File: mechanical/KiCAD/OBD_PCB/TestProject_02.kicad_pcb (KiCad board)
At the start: 2 copper layers, 41 x 58 mm, 46 parts, among them J1 USB_C_Receptacle_USB2.0_16P, J2 C-OBD-II-16M, J3 TXD_PAD, J4 RXD_PAD, U1 ESP32-C3-WROOM-02, U2 TPS54302, U3 USBLC6-2P6, U4 SN65HVD231

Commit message: Small layout changes, relocated the OBD PCB files to it's own folder. Final checks are needed.
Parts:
- moved C8 0.60 mm to (84.7, 54.4)
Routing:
- net OPMODE: track 36.3 -> 37.4 mm
- net +3.3V: track 94.7 -> 95.7 mm
- net Net-(J1-SHIELD): track 24.6 -> 25.3 mm
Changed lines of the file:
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@@
 	(footprint "Capacitor_SMD:C_0603_1608Metric"
 		(layer "B.Cu")
-		(at 84.65 53.8)
+		(at 84.7 54.4)
 		(descr "Capacitor SMD 0603 (1608 Metric), square (rectangular) end terminal, IPC-7351 nominal, (Body size source: IPC-SM-782 page 76, https://www.pcb-3d.com/wordpress/wp-content/uploads/ipc-sm-782a_amendment_1_and_2.pdf)")
 		(tags "capacitor")
@@
 		(layer "F.Fab")
 		(pts
-			(xy 46 50.4) (xy 46 97.85)
+			(xy 46 50.4) (xy 45.25 98)
 		)
 		(height -5)
@@
 			(extension_offset 0.5)
 		)
-		(gr_text "47.45mm"
-			(at 39.85 74.125 0)
+		(gr_text "47.6mm"
+			(at 39.85 74.2 0)
+			(layer "F.Fab")
+			(effects
+				(font
+					(size 1 1)
+					(thickness 0.15)
+				)
+			)
+		)
+	)
+	(dimension
+		(type orthogonal)
+		(layer "F.Fab")
+		(pts
+			(xy 87.5 119) (xy 86.75 40)
+		)
+		(height 5)
+		(orientation 1)
+		(format
+			(prefix "")
+			(suffix "mm")
+			(units 3)
+			(units_format 0)
+			(precision 4)
+			(suppress_zeroes yes)
+		)
+		(style
+			(thickness 0.05)
+			(arrow_length 1.27)
+			(text_position_mode 0)
+			(arrow_direction outward)
+			(extension_height 0.58642)
+			(extension_offset 0.5)
+		)
+		(gr_text "79mm"
+			(at 91.35 79.5 0)
 			(layer "F.Fab")
 			(effects
@@
 		(layer "F.Fab")
 		(pts
-			(xy 87 98) (xy 87 40)
+			(xy 92.5 98) (xy 92.5 40)
 		)
 		(height 5)
@@
 		)
 		(gr_text "58mm"
-			(at 90.85 69 0)
+			(at 96.35 69 0)
 			(layer "F.Fab")
 			(effects
@@
 	)
 	(segment
-		(start 49.3875 66.7)
-		(end 49.3875 75.55)
-		(width 0.5)
-		(layer "F.Cu")
-		(net "+3.3V")
-	)
-	(segment
-		(start 66.4125 70.6)
-		(end 66.4125 80.4875)
+		(start 65.45 83.3)
+		(end 63.6 83.3)
 		(width 0.5)
 		(layer "F.Cu")
@@
 	)
 	(segment
-		(start 63.6 83.3)
-		(end 61.4 85.5)
+		(start 49.3875 66.7)
+		(end 49.3875 75.55)
 		(width 0.5)
 		(layer "F.Cu")
@@
 	)
 	(segment
+		(start 67.5 85.35)
+		(end 65.45 83.3)
+		(width 0.5)
+		(layer "F.Cu")
+		(net "+3.3V")
+	)
+	(segment
+		(start 69.6 85.35)
+		(end 67.5 85.35)
+		(width 0.5)
+		(layer "F.Cu")
+		(net "+3.3V")
+	)
+	(segment
 		(start 49.3875 75.55)
 		(end 49.3875 80.9875)
@@
 	)
 	(segment
-		(start 49.3875 80.9875)
-		(end 51.7 83.3)
+		(start 66.4125 70.6)
+		(end 66.4125 82.3375)
 		(width 0.5)
 		(layer "F.Cu")
@@
 	)
 	(segment
-		(start 69.6 85.35)
-		(end 65.65 85.35)
+		(start 49.3875 80.9875)
+		(end 51.7 83.3)
 		(width 0.5)
 		(layer "F.Cu")
@@
 	)
 	(segment
-		(start 66.4125 80.4875)
-		(end 63.6 83.3)
-		(width 0.5)
-		(layer "F.Cu")
-		(net "+3.3V")
-	)
-	(segment
-		(start 61.4 85.5)
-		(end 61 85.5)
+		(start 63.25 85.5)
+		(end 65.45 83.3)
 		(width 0.5)
 		(layer "F.Cu")
@@
 	)
 	(segment
-		(start 65.65 85.35)
-		(end 63.6 83.3)
+		(start 66.4125 82.3375)
+		(end 65.45 83.3)
+		(width 0.5)
+		(layer "F.Cu")
+		(net "+3.3V")
+	)
+	(segment
+		(start 61 85.5)
+		(end 63.25 85.5)
 		(width 0.5)
 		(layer "F.Cu")
@@
 	)
 	(segment
-		(start 85.425 53.8)
-		(end 85.425 51.1125)
+		(start 85.425 51.1125)
+		(end 85.4125 51.1)
 		(width 0.5)
 		(layer "B.Cu")
@@
 	)
 	(segment
-		(start 76.79 42.425)
-		(end 85.43 42.425)
+		(start 85.475 54.4)
+		(end 85.425 54.35)
 		(width 0.5)
 		(layer "B.Cu")
@@
 	)
 	(segment
-		(start 85.425 51.1125)
-		(end 85.4125 51.1)
+		(start 76.79 42.425)
+		(end 85.43 42.425)
 		(width 0.5)
 		(layer "B.Cu")
@@
 	)
 	(segment
+		(start 85.425 54.35)
+		(end 85.425 51.1125)
+		(width 0.5)
+		(layer "B.Cu")
+		(net "Net-(J1-SHIELD)")
+	)
+	(segment
 		(start 72.6 96)
 		(end 70.6 94)
@@
 	)
 	(segment
-		(start 49.895 83.075)
-		(end 49.895 82.100001)
+		(start 72 63.2)
+		(end 71.5 63.2)
 		(width 0.25)
 		(layer "B.Cu")
@@
 	)
 	(segment
-		(start 60 81.2)
-		(end 71.5 69.7)
+		(start 72.5 63.7)
+		(end 72 63.2)
 		(width 0.25)
 		(layer "B.Cu")
@@
 	)
 	(segment
-		(start 71.5 69.7)
-		(end 71.5 63.2)
+		(start 50.795001 81.2)
+		(end 60 81.2)
 		(width 0.25)
 		(layer "B.Cu")
@@
 	)
 	(segment
-		(start 50.795001 81.2)
-		(end 60 81.2)
+		(start 49.895 83.075)
+		(end 49.895 82.100001)
 		(width 0.25)
 		(layer "B.Cu")
@@
 		(width 0.25)
 		(layer "B.Cu")
+		(net "OPMODE")
+	)
+	(segment
+		(start 60 81.2)
+		(end 72.5 68.7)
+		(width 0.25)
+		(layer "B.Cu")
+		(net "OPMODE")
+	)
+	(segment
+		(start 72.5 68.7)
+		(end 72.5 63.7)
+		(width 0.25)
+		(layer "B.Cu")

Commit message: Touch ups, finalizing component placements
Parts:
- J2: footprint C-OBD-II-16M:COMTECH_C-OBD-II-16M -> custom_library:COMTECH_C-OBD-II-16M
- moved J4 19.8 mm to (60.6, 71.0)
- moved J3 13.6 mm to (65.1, 71.0)
- moved D1 2.46 mm to (79.8, 56.8)
- moved D2 2.45 mm to (84.5, 56.8)
- moved C8 2.40 mm to (84.7, 52.0)
- moved R6 2.35 mm to (84.5, 48.8)
- moved U3 2.18 mm to (78.5, 50.2)
- moved C7 2.06 mm to (76.5, 59.5)
- moved F1 2.02 mm to (83.5, 49.8)
- moved J1 2.00 mm to (81.2, 41.5)
- moved MountingHole 1.76 mm to (78.1, 67.0)
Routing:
- net Net-(J4-Pin_1): track 6.98 -> 14.6 mm
- net Net-(J3-Pin_1): track 4.67 -> 11.4 mm
- net VIN: track 31.2 -> 33.6 mm
- net Net-(J1-CC2): track 6.59 -> 8.47 mm
- net Net-(J1-CC1): track 6.65 -> 8.15 mm
- net OPMODE: track 37.4 -> 36.5 mm
- net /D+: track 6.84 -> 7.73 mm
- net Net-(J1-SHIELD): track 25.3 -> 24.4 mm
- net /D-: track 5.85 -> 6.70 mm
- net USB_D+: track 11.7 -> 11.0 mm
- net USB_D-: track 13.6 -> 13.1 mm
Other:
- board size 41 x 58 mm -> 41 x 59.1 mm

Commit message: Started the display PCB, since i use QSPI the current pinouts are not correct. Some ICs are still missing or not yet intergrated.
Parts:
- J2: footprint custom_library:COMTECH_C-OBD-II-16M -> C-OBD-II-16M:COMTECH_C-OBD-II-16M
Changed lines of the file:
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@@
 		)
 	)
-	(footprint "custom_library:COMTECH_C-OBD-II-16M"
+	(footprint "C-OBD-II-16M:COMTECH_C-OBD-II-16M"
 		(layer "F.Cu")
 		(at 52.6 96)
@@
 		)
 		(embedded_fonts no)
-		(model "C:/Users/User/Documents/KiCad/10.0/custom_library/C-OBD-II-16M.step"
+		(model "C:/Users/Acrob/Desktop/C-OBD-II-16M/C-OBD-II-16M.step"
 			(offset
 				(xyz 0 0 -2.5)
@@
 			(extension_offset 0.5)
 		)
-		(gr_text "47.85mm"
+		(gr_text "47,85mm"
 			(at 39.85 74.075 0)
 			(layer "F.Fab")
@@
 			(extension_offset 0.5)
 		)
-		(gr_text "80.1mm"
+		(gr_text "80,1mm"
 			(at 91.35 78.95 0)
 			(layer "F.Fab")
@@
 			(keep_text_aligned yes)
 		)
-		(gr_text "29.2mm"
+		(gr_text "29,2mm"
 			(at 60.6 33.25 0)
 			(layer "F.Fab")
@@
 			(keep_text_aligned yes)
 		)
-		(gr_text "41.8mm"
+		(gr_text "41,8mm"
 			(at 66.6 122.85 0)
 			(layer "F.Fab")
@@
 			(extension_offset 0.5)
 		)
-		(gr_text "11.15mm"
+		(gr_text "11,15mm"
 			(at 39.85 44.575 0)
 			(layer "F.Fab")
@@
 			(extension_offset 0.5)
 		)
-		(gr_text "59.1mm"
+		(gr_text "59,1mm"
 			(at 96.35 68.45 0)
 			(layer "F.Fab")
@@
 			(keep_text_aligned yes)
 		)
-		(gr_text "11.8mm"
+		(gr_text "11,8mm"
 			(at 81.1 33.253553 0)
 			(layer "F.Fab")

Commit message: Display schematic is finished, footprints are assigned, the basic board shape has been made, now the components has to be placed.
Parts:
- C4: value 100 nF -> 10 uF
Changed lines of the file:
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@@
 			)
 		)
-		(property "Value" "100 nF"
+		(property "Value" "10 uF"
 			(at 0 1.68 0)
 			(layer "F.Fab")
@@
 			(extension_offset 0.5)
 		)
-		(gr_text "47,85mm"
+		(gr_text "47.85mm"
 			(at 39.85 74.075 0)
 			(layer "F.Fab")
@@
 			(extension_offset 0.5)
 		)
-		(gr_text "80,1mm"
+		(gr_text "80.1mm"
 			(at 91.35 78.95 0)
 			(layer "F.Fab")
@@
 			(keep_text_aligned yes)
 		)
-		(gr_text "29,2mm"
+		(gr_text "29.2mm"
 			(at 60.6 33.25 0)
 			(layer "F.Fab")
@@
 			(keep_text_aligned yes)
 		)
-		(gr_text "41,8mm"
+		(gr_text "41.8mm"
 			(at 66.6 122.85 0)
 			(layer "F.Fab")
@@
 			(extension_offset 0.5)
 		)
-		(gr_text "11,15mm"
+		(gr_text "11.15mm"
 			(at 39.85 44.575 0)
 			(layer "F.Fab")
@@
 			(extension_offset 0.5)
 		)
-		(gr_text "59,1mm"
+		(gr_text "59.1mm"
 			(at 96.35 68.45 0)
 			(layer "F.Fab")
@@
 			(keep_text_aligned yes)
 		)
-		(gr_text "11,8mm"
+		(gr_text "11.8mm"
 			(at 81.1 33.253553 0)
 			(layer "F.Fab")

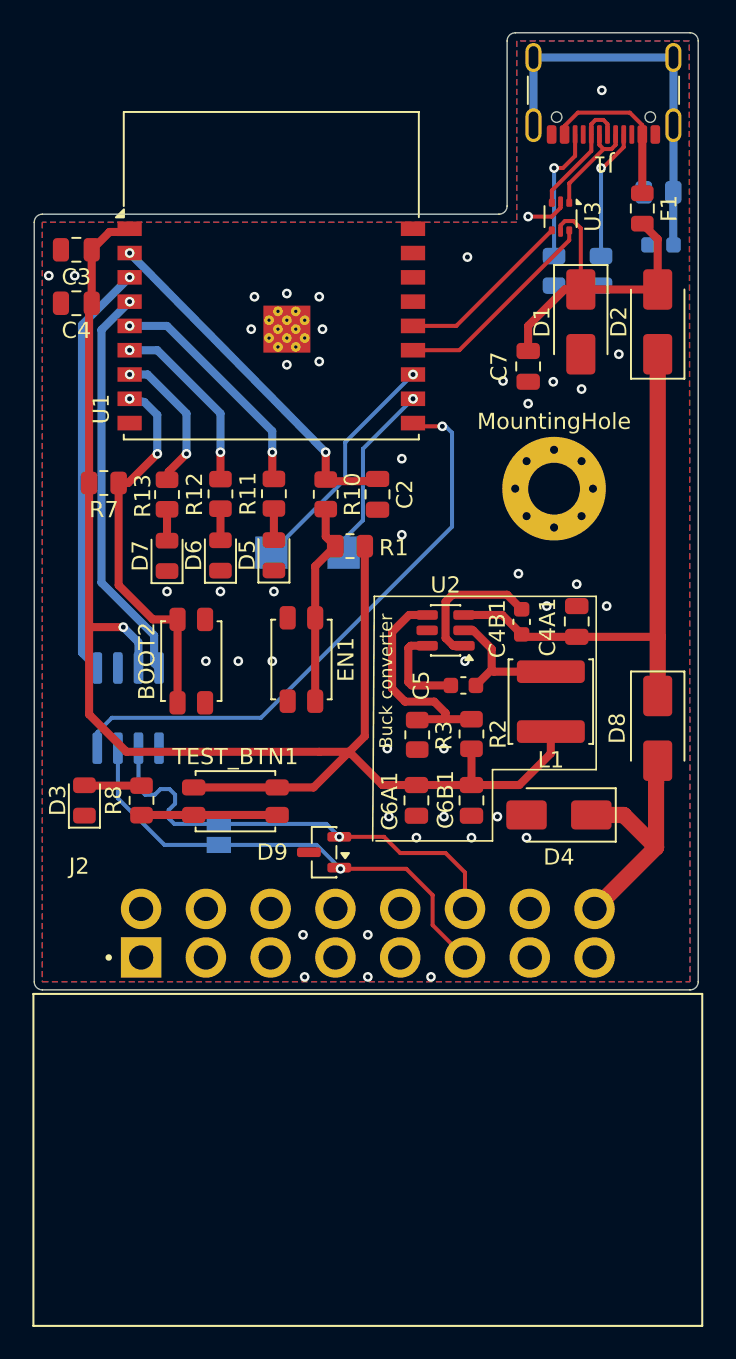
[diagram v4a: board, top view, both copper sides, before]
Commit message: OBD and displa PCB are both basically finished, some files has to be generated and the PCBs can be ordered. Documentation should be the next step.
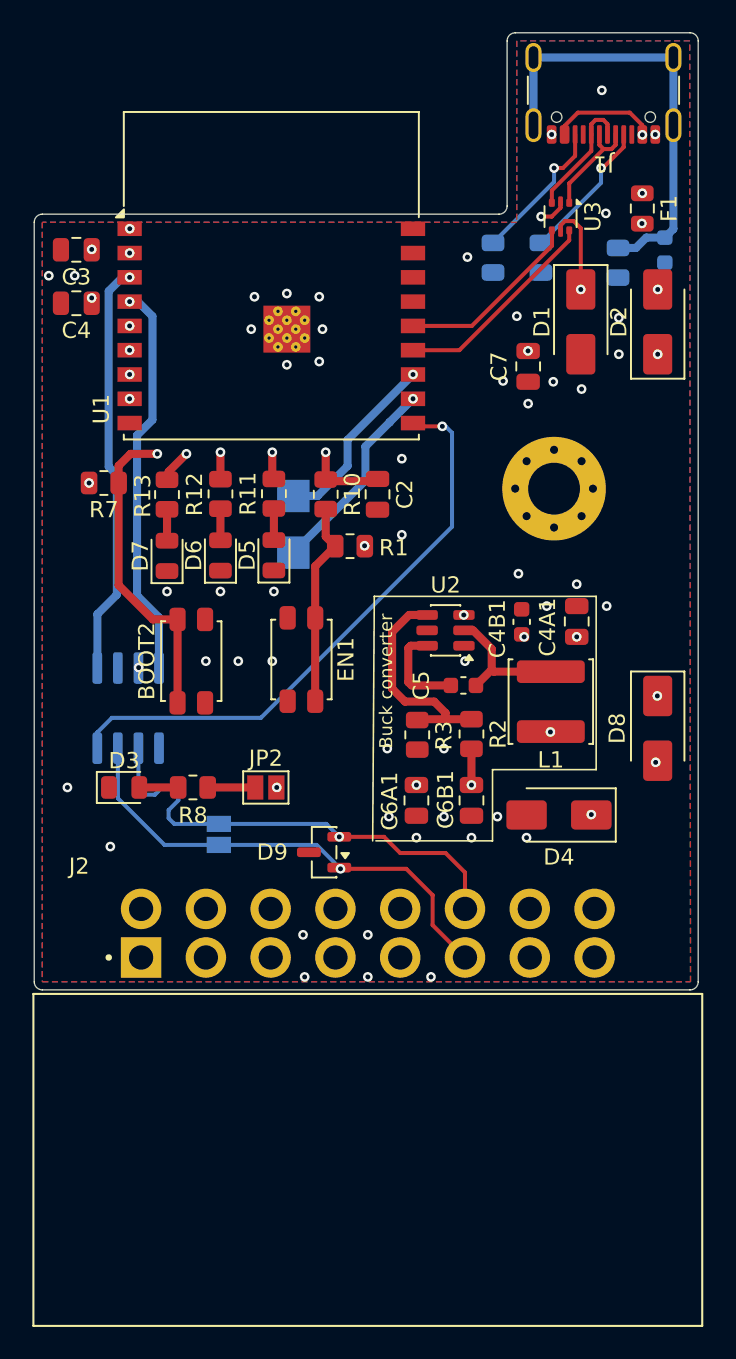
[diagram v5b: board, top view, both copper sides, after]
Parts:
- removed TEST_BTN1: SW_MEC_5E, Button_Switch_SMD:SW_SPST_EVQP2_MiddlePushTravel_H2.5mm
- added JP2: SolderJumper_2_Open, Jumper:SolderJumper-2_P1.3mm_Open_Pad1.0x1.5mm, F.Cu at (60.3, 85.5)
- MountingHole: moved to B.Cu
- moved R6 5.02 mm to (82.0, 53.1), turned to -90 degrees
- moved R5 3.86 mm to (74.3, 52.8)
- moved R4 3.80 mm to (77.3, 52.8)
- moved J4 3.75 mm to (62.0, 67.5)
- moved R8 3.27 mm to (55.8, 85.5), turned to 0 degrees
- moved J3 3.10 mm to (62.0, 71.0)
- moved D3 2.58 mm to (51.5, 85.5), turned to 0 degrees
- moved C8 0.40 mm to (84.9, 52.3), turned to 90 degrees
- turned MountingHole to 180 degrees
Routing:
- net GND: track 11.4 -> 1.81 mm, vias 43 -> 50
- net Net-(JP2-A): track 8.38 -> 2.94 mm
- net +3.3V: track 95.7 -> 91.0 mm, vias 1 -> 10
- net Net-(J1-SHIELD): track 24.4 -> 27.9 mm
- net Net-(J4-Pin_1): track 14.6 -> 11.4 mm
- net Net-(D3-A): track 3.54 -> 2.40 mm
- net Net-(J3-Pin_1): track 11.4 -> 12.6 mm
- net Net-(J1-CC2): track 8.47 -> 9.22 mm
- net Net-(J1-CC1): track 8.15 -> 8.88 mm
- net BOOT: track 23.6 -> 24.3 mm
- net USB_D+: track 11.0 -> 11.6 mm
- net CANL: track 29.8 -> 30.3 mm
- net VIN: track 33.6 -> 33.9 mm, vias 0 -> 5
- net Net-(D4-A1): track 15.6 -> 15.5 mm, vias 0 -> 2
- net Net-(D1-A1): track 20.6 -> 20.7 mm, vias 0 -> 4
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- added copper zone on In1.Cu, net GND
- added copper zone on In2.Cu, net GND
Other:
- copper layers 2 -> 4

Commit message: PCBs should be finished, they can be ordered. The plan was to finish the PCB design about a week ago. I already have the display and got two ESP devboard so i can start the software and test it.
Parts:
- C2, C3, C5: value 0.1 uF -> 100nF
- C4: value 10 uF -> 10uF
- JP2: value SolderJumper_2_Open -> Power Line Tester
- R10, R11, R12, R13: footprint Resistor_SMD:R_0805_2012Metric -> Resistor_SMD:R_0603_1608Metric
- moved R4 2.35 mm to (79.6, 53.2)
- moved R5 2.11 mm to (76.4, 53.2)
- moved C2 0.12 mm to (67.2, 67.5)
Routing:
- net +3.3V: track 91.0 -> 95.4 mm, vias 10 -> 6
- net Net-(J4-Pin_1): track 11.4 -> 15.0 mm
- net Net-(J3-Pin_1): track 12.6 -> 16.1 mm
- net CAN_RX: track 24.7 -> 26.6 mm
- net EN: track 22.2 -> 23.2 mm
- net CANL: track 30.3 -> 30.9 mm
- net Net-(J1-CC1): track 8.88 -> 8.33 mm
- net VIN: track 33.9 -> 33.6 mm, vias 5 -> 3
- net Net-(D1-A1): track 20.7 -> 20.6 mm, vias 4 -> 0
- net Net-(F1-Pad1): vias 2 -> 0
- net GND: vias 50 -> 67

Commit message: Small changes due to via and silkscreen overlaps, moved every via-in-pad seperately from soldering pad. PCBs have been ordered. Some problems occured with the buttons since the ones i chose had a 5th mounting pin which was not present on the PCB. Also they asked about the button polarity and placement.Everything was corrected and the order moved to production.
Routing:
- net GND: track 1.81 -> 4.72 mm, vias 67 -> 68
